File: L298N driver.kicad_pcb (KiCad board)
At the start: 2 copper layers, 75 x 75 mm, 39 parts, among them J1 Screw_Terminal_01x03, J2 Conn_01x02_Pin, J3 Conn_01x05, J4 Conn_01x05, J5 Conn_01x02, J6 Conn_01x02, J7 Conn_01x02, J8 Conn_01x02, U1 74HC595, U2 LM78M05_TO220, U3 DEV-15795, U4 L298N, U5 L298N

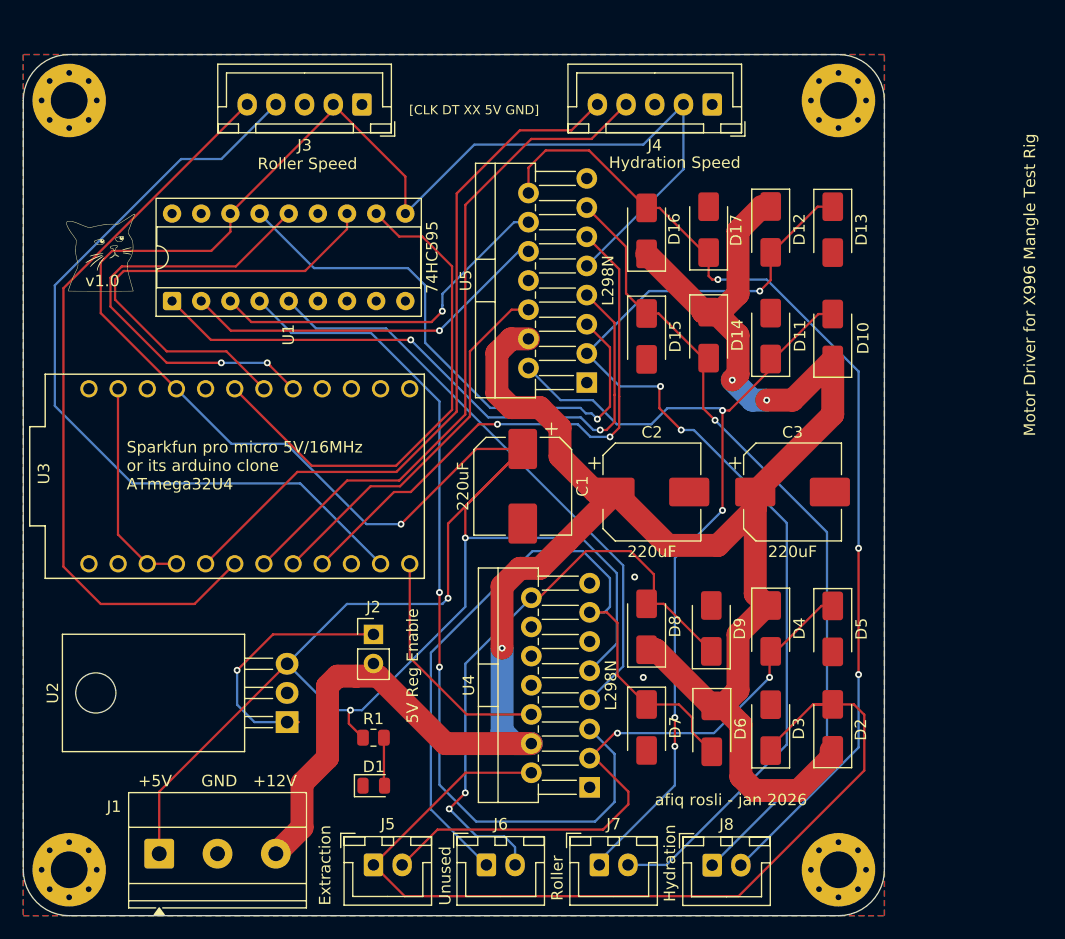
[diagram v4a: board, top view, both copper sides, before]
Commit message: fat OUT traces
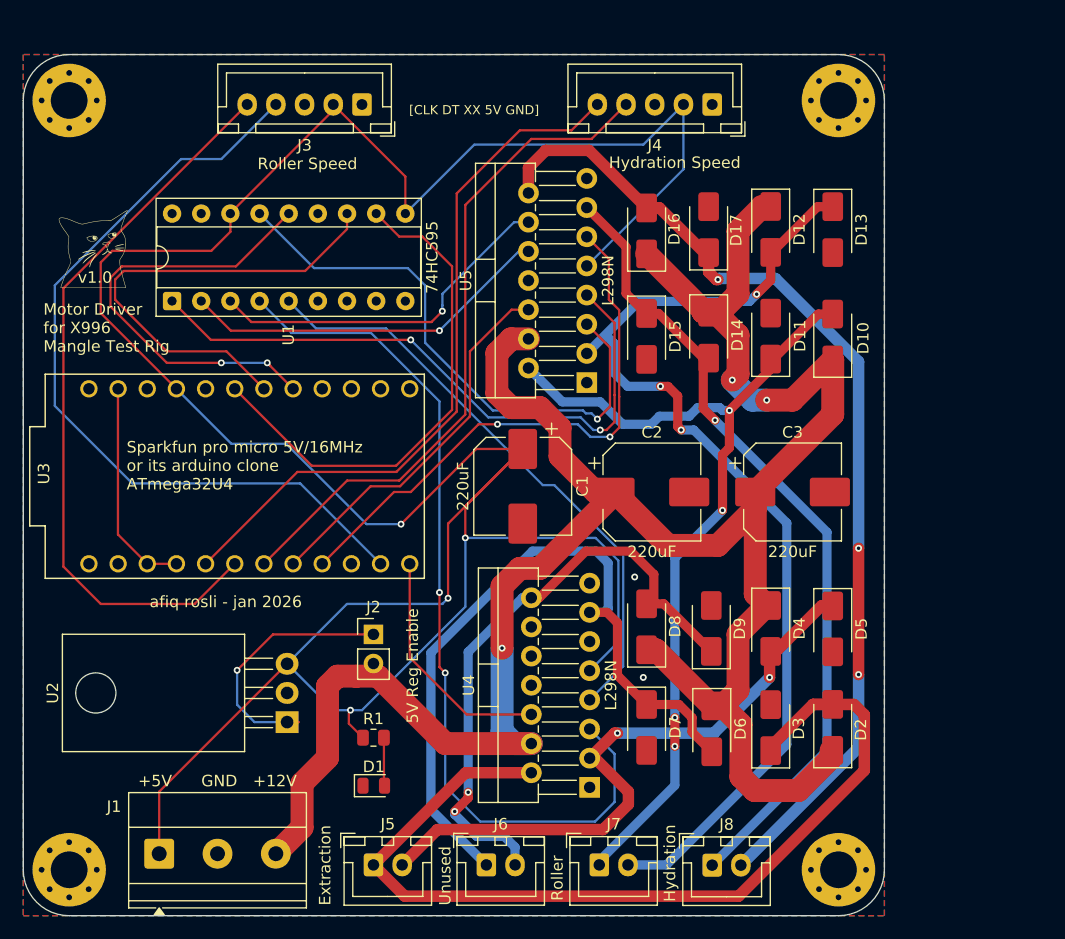
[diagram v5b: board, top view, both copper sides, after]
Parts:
- moved G*** 0.72 mm to (66.1, 77.0)
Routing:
- net +5V: track 253.1 -> 253.9 mm
- net /extraction_in2: track 51.6 -> 52.2 mm
- net Net-(D6-A): track 64.3 -> 64.8 mm

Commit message: fine tune traces
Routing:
- net Net-(D2-A): track 81.6 -> 83.4 mm
- net +5V: track 253.9 -> 255.0 mm
- net /rotary_enc_roller_dt: track 70.3 -> 71.3 mm
- net VCC: track 203.0 -> 204.0 mm
- net /clk: track 44.7 -> 45.5 mm
- net /data: track 39.2 -> 39.8 mm
- net /roller_in1: track 49.3 -> 49.9 mm

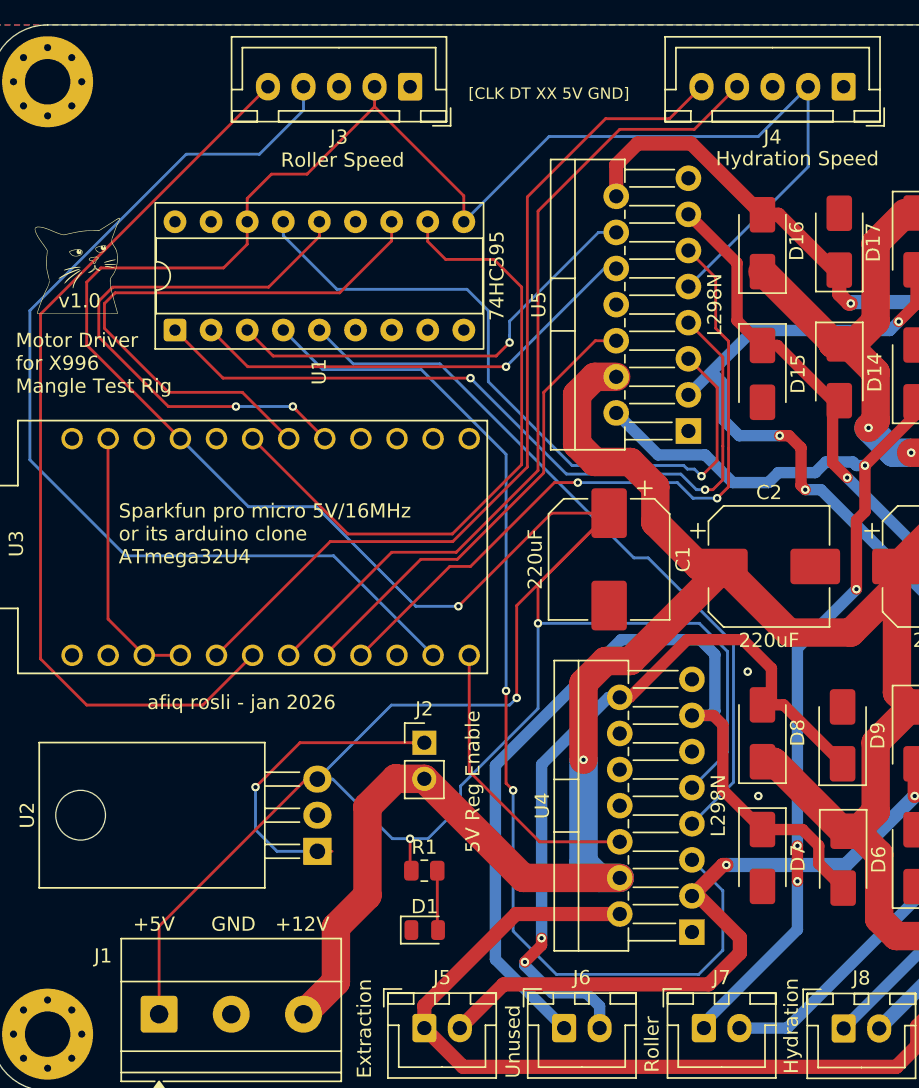
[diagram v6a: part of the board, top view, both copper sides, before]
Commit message: correct shift register to DIP-16 and power net trace width
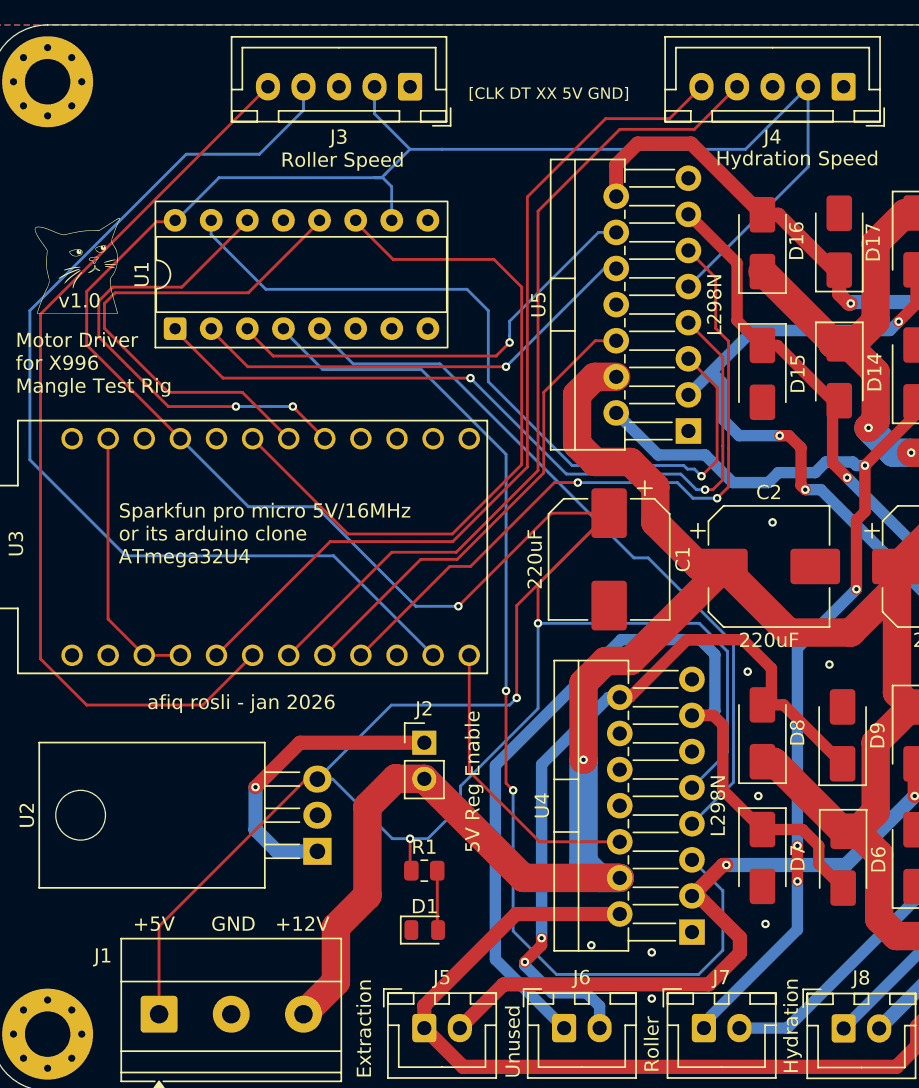
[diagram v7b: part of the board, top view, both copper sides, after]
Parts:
- U1: footprint Package_DIP:DIP-18_W7.62mm_Socket -> Package_DIP:DIP-16_W7.62mm_Socket
- moved U1 0.10 mm to (73.0, 81.4)
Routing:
- net /latch: track 41.3 -> 35.4 mm
- net /data: track 39.8 -> 34.1 mm
- net /roller_in1: track 49.9 -> 54.9 mm
- net /clk: track 45.5 -> 49.8 mm
- net +5V: track 255.0 -> 253.4 mm
- net /power: track 22.2 -> 21.2 mm
- net GND: vias 2 -> 8
